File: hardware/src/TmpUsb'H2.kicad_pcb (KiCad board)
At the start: 2 copper layers, 26.5 x 17 mm, 20 parts, among them J1 215307, J2 292133-3, U1 PIC18F26J50

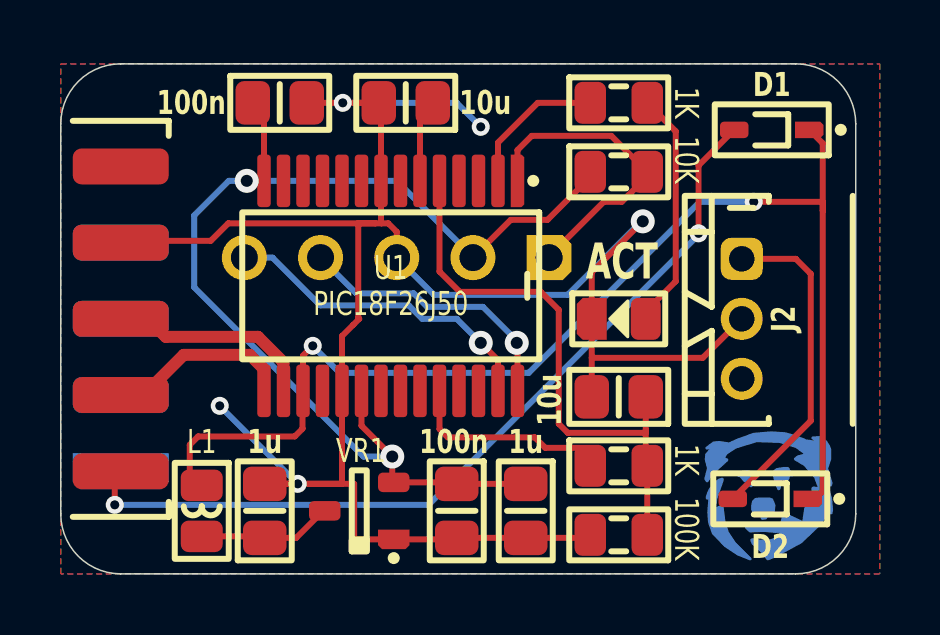
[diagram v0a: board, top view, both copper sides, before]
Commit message: Renamed V+ nets
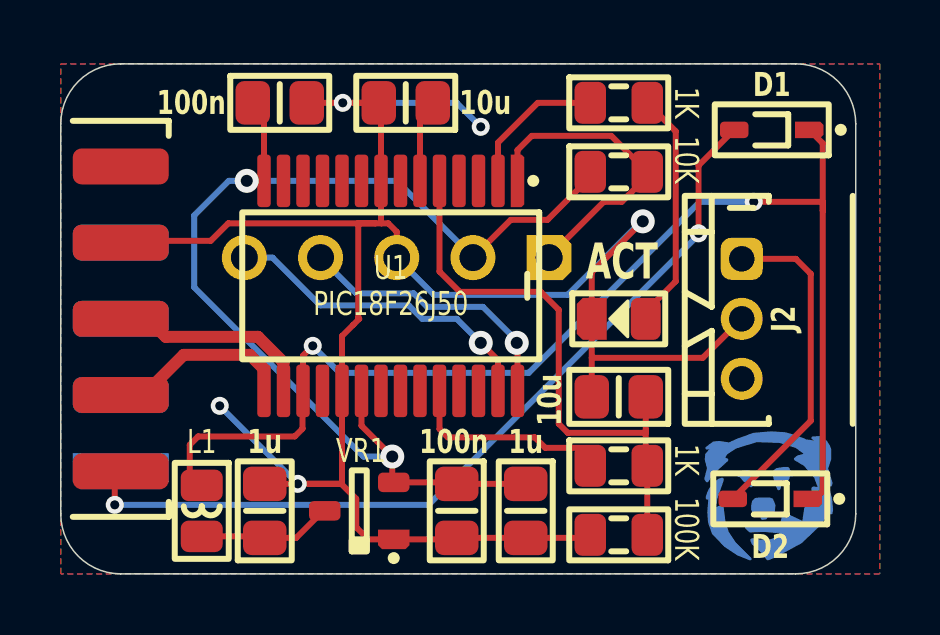
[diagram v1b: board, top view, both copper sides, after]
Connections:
- net +3.3V renamed 3V3
- net +5V renamed 5V
- net VCAP renamed 3V3_VCAP
- net VCC renamed 5V_IN
- net Vstby renamed 5V_STBY
- net Vusb renamed 5V_USB
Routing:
- net GND: track 74.4 -> 71.3 mm

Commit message: Swapping diodes around
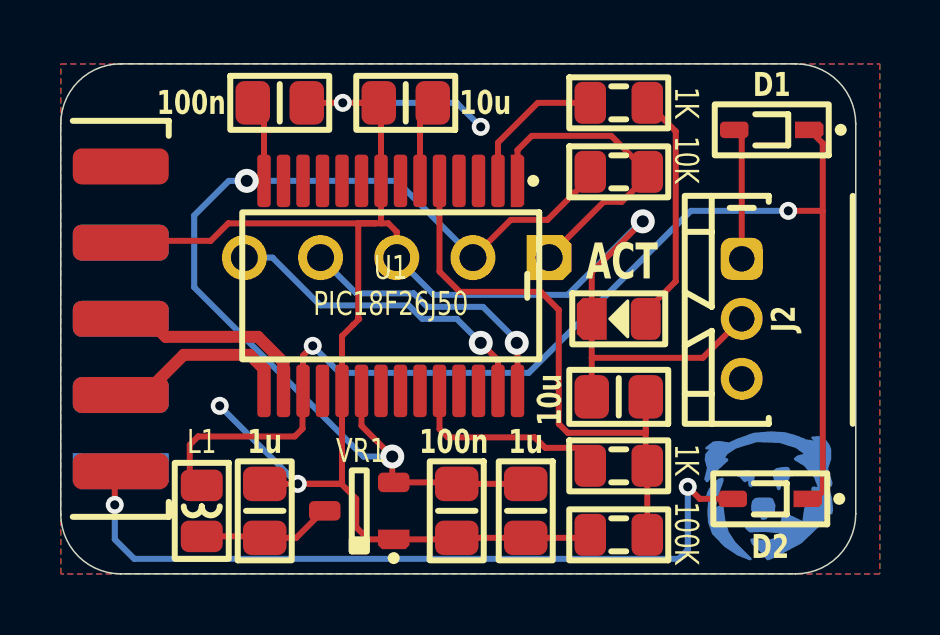
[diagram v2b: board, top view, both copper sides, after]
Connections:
- D1 pad 2: 5V_USB -> 5V_STBY
- D2 pad 2: 5V_STBY -> 5V_USB
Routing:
- net 5V_STBY: track 11.1 -> 4.40 mm
- net 5V_USB: track 28.3 -> 25.5 mm
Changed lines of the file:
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@@
 		)
 		(property "Value" "100K"
-			(at -2.25 0.2 -90)
+			(at -2.25 0.05 270)
 			(unlocked yes)
 			(layer "F.SilkS")
@@
 			(layers "F.Cu" "F.Paste" "F.Mask")
 			(roundrect_rratio 0.25)
-			(net 11 "5V_USB")
+			(net 15 "5V_STBY")
 			(thermal_bridge_angle 45)
 		)
@@
 			(layers "F.Cu" "F.Paste" "F.Mask")
 			(roundrect_rratio 0.25)
-			(net 15 "5V_STBY")
+			(net 11 "5V_USB")
 			(thermal_bridge_angle 45)
 		)
@@
 	)
 	(gr_text "TmpUsb'H2 BXXXX"
-		(at 28.2 30.7 0)
+		(at 26.2 23.9 0)
 		(layer "B.SilkS")
 		(effects
@@
 	)
 	(segment
-		(start 36.260361 18.389639)
-		(end 36.260361 20.65)
+		(start 36.3 29.5)
+		(end 35.9 29.1)
 		(width 0.2)
 		(layer "F.Cu")
@@
 	)
 	(segment
-		(start 37.45 17.2)
-		(end 36.260361 18.389639)
+		(start 37.4 29.5)
+		(end 36.3 29.5)
 		(width 0.2)
 		(layer "F.Cu")
@@
 	)
 	(via
-		(at 36.260361 20.65)
+		(at 35.9 29.1)
 		(size 0.6)
 		(drill 0.3)
@@
 	)
 	(segment
-		(start 36.260361 20.7003)
-		(end 36.260361 20.65)
+		(start 35.6 31.5)
+		(end 35.9 31.2)
+		(width 0.2)
+		(layer "B.Cu")
+		(net 11)
+	)
+	(segment
+		(start 35.9 31.2)
+		(end 35.9 29.1)
 		(width 0.2)
 		(layer "B.Cu")
@@
 	(segment
 		(start 16.8 29.7)
-		(end 27.260661 29.7)
+		(end 16.8 30.85)
 		(width 0.2)
 		(layer "B.Cu")
@@
 	)
 	(segment
-		(start 27.260661 29.7)
-		(end 36.260361 20.7003)
+		(start 17.45 31.5)
+		(end 35.6 31.5)
+		(width 0.2)
+		(layer "B.Cu")
+		(net 11)
+	)
+	(segment
+		(start 16.8 30.85)
+		(end 17.45 31.5)
 		(width 0.2)
 		(layer "B.Cu")
@@
 	)
 	(segment
-		(start 37.7 21.5)
-		(end 39.5 21.5)
-		(width 0.2)
-		(layer "F.Cu")
-		(net 15)
-	)
-	(segment
-		(start 39.5 21.5)
-		(end 40 22)
+		(start 37.7 17.45)
+		(end 37.45 17.2)
 		(width 0.2)
 		(layer "F.Cu")
@@
 	)
 	(segment
-		(start 40 22)
-		(end 40 26.9)
-		(width 0.2)
-		(layer "F.Cu")
-		(net 15)
-	)
-	(segment
-		(start 40 26.9)
-		(end 37.4 29.5)
+		(start 37.7 21.5)
+		(end 37.7 17.45)
 		(width 0.2)
 		(layer "F.Cu")
@@
 	)
 	(segment
-		(start 40.4 19.6)
-		(end 38.1 19.6)
+		(start 40.4 19.9)
+		(end 39.250008 19.9)
 		(width 0.2)
 		(layer "F.Cu")
@@
 	)
 	(segment
-		(start 40.4 19.9)
-		(end 40.4 19.6)
+		(start 39.250008 19.9)
+		(end 39.25 19.899992)
 		(width 0.2)
 		(layer "F.Cu")
@@
 	)
 	(via
-		(at 38.1 19.6)
+		(at 39.25 19.899992)
 		(size 0.6)
 		(drill 0.3)
@@
 	)
 	(segment
-		(start 36.3 19.6)
-		(end 38.1 19.6)
+		(start 24.3 25.3)
+		(end 30.6 25.3)
 		(width 0.2)
 		(layer "B.Cu")
@@
 	)
 	(segment
-		(start 24.3 25.3)
-		(end 30.6 25.3)
+		(start 30.6 25.3)
+		(end 36.000008 19.899992)
 		(width 0.2)
 		(layer "B.Cu")
@@
 	)
 	(segment
-		(start 30.6 25.3)
-		(end 36.3 19.6)
+		(start 36.000008 19.899992)
+		(end 39.25 19.899992)
 		(width 0.2)
 		(layer "B.Cu")

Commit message: Adjusted silkscreen
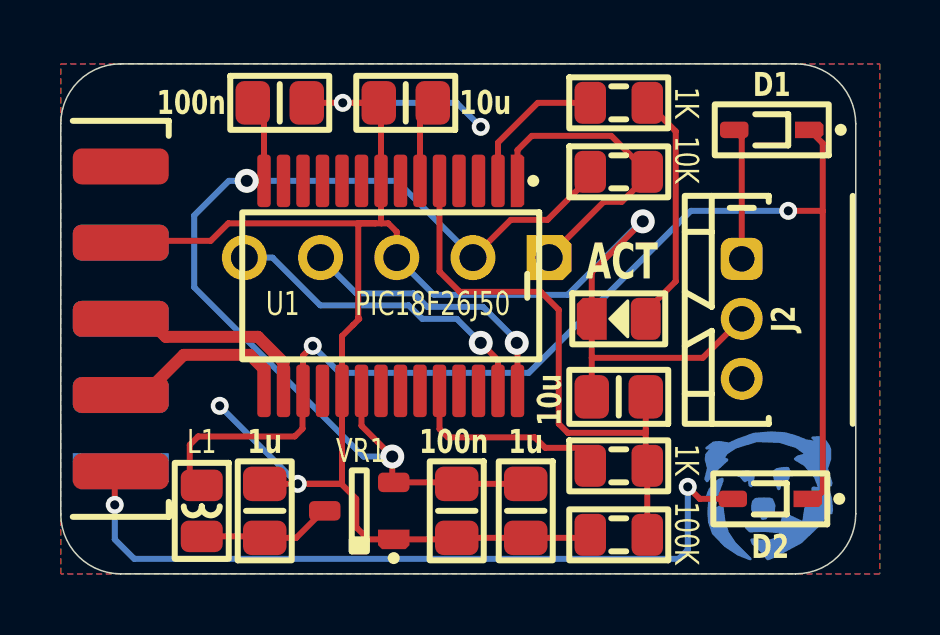
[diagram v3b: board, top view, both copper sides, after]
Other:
- board text added: "5V"
- board text added: "GND"
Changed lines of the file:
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@@
 		)
 		(property "Value" "100K"
-			(at -2.25 0.05 270)
+			(at -2.25 0.05 -90)
 			(unlocked yes)
 			(layer "F.SilkS")
@@
 				(font
 					(size 1.27 1.27)
+					(thickness 0.15)
 				)
 			)
@@
 				(font
 					(size 1.27 1.27)
+					(thickness 0.15)
 				)
 			)
@@
 				(font
 					(size 1.27 1.27)
+					(thickness 0.15)
 				)
 			)
@@
 				(font
 					(size 1.27 1.27)
+					(thickness 0.15)
 				)
 			)
@@
 				(font
 					(size 1.27 1.27)
+					(thickness 0.15)
 				)
 			)
@@
 				(font
 					(size 1.27 1.27)
+					(thickness 0.15)
 				)
 			)
@@
 				(font
 					(size 1.27 1.27)
+					(thickness 0.15)
 				)
 			)
@@
 				(font
 					(size 1.27 1.27)
+					(thickness 0.15)
 				)
 			)
@@
 				(font
 					(size 1.27 1.27)
+					(thickness 0.15)
 				)
 			)
@@
 				(font
 					(size 1.27 1.27)
+					(thickness 0.15)
 				)
 			)
@@
 				(font
 					(size 1.27 1.27)
+					(thickness 0.15)
 				)
 			)
@@
 				(font
 					(size 1.27 1.27)
+					(thickness 0.15)
 				)
 			)
@@
 				(font
 					(size 1.27 1.27)
+					(thickness 0.15)
 				)
 			)
@@
 				(font
 					(size 1.27 1.27)
+					(thickness 0.15)
 				)
 			)
@@
 				(font
 					(size 1.27 1.27)
+					(thickness 0.15)
 				)
 			)
@@
 				(font
 					(size 1.27 1.27)
+					(thickness 0.15)
 				)
 			)
@@
 				(font
 					(size 1.27 1.27)
+					(thickness 0.15)
 				)
 			)
@@
 				(font
 					(size 1.27 1.27)
+					(thickness 0.15)
 				)
 			)
@@
 				(font
 					(size 1.27 1.27)
+					(thickness 0.15)
 				)
 			)
@@
 				(font
 					(size 1.27 1.27)
+					(thickness 0.15)
 				)
 			)
@@
 				(font
 					(size 1.27 1.27)
+					(thickness 0.15)
 				)
 			)
@@
 				(font
 					(size 1.27 1.27)
+					(thickness 0.15)
 				)
 			)
@@
 				(font
 					(size 1.27 1.27)
+					(thickness 0.15)
 				)
 			)
@@
 				(font
 					(size 1.27 1.27)
+					(thickness 0.15)
 				)
 			)
@@
 				(font
 					(size 1.27 1.27)
+					(thickness 0.15)
 				)
 			)
@@
 				(font
 					(size 1.27 1.27)
+					(thickness 0.15)
 				)
 			)
@@
 				(font
 					(size 1.27 1.27)
+					(thickness 0.15)
 				)
 			)
@@
 				(font
 					(size 1.27 1.27)
+					(thickness 0.15)
 				)
 			)
@@
 				(font
 					(size 1.27 1.27)
+					(thickness 0.15)
 				)
 			)
@@
 				(font
 					(size 1.27 1.27)
+					(thickness 0.15)
 				)
 			)
@@
 				(font
 					(size 1.27 1.27)
+					(thickness 0.15)
 				)
 			)
@@
 				(font
 					(size 1.27 1.27)
+					(thickness 0.15)
 				)
 			)
@@
 				(font
 					(size 1.27 1.27)
+					(thickness 0.15)
 				)
 			)
@@
 				(font
 					(size 1.27 1.27)
+					(thickness 0.15)
 				)
 			)
@@
 				(font
 					(size 1.27 1.27)
+					(thickness 0.15)
 				)
 			)
@@
 				(font
 					(size 1.27 1.27)
+					(thickness 0.15)
 				)
 			)
@@
 				(font
 					(size 1.27 1.27)
+					(thickness 0.15)
 				)
 			)
@@
 				(font
 					(size 1.27 1.27)
+					(thickness 0.15)
 				)
 			)
@@
 				(font
 					(size 1.27 1.27)
+					(thickness 0.15)
 				)
 			)
@@
 				(font
 					(size 1.27 1.27)
+					(thickness 0.15)
 				)
 			)
@@
 				(font
 					(size 1.27 1.27)
+					(thickness 0.15)
 				)
 			)
@@
 				(font
 					(size 1.27 1.27)
+					(thickness 0.15)
 				)
 			)
@@
 		(tags "SOP65P775X200-28N")
 		(property "Reference" "U1"
-			(at -0.6 0 0)
+			(at 0.6 3.6 0)
 			(layer "F.SilkS")
 			(effects
@@
 		)
 		(property "Value" "PIC18F26J50"
-			(at 0.6 0 0)
+			(at 0.6 -1.4 0)
 			(layer "F.SilkS")
 			(effects
@@
 				(font
 					(size 1.27 1.27)
+					(thickness 0.15)
 				)
 			)
@@
 				(font
 					(size 1.27 1.27)
+					(thickness 0.15)
 				)
 			)
@@
 				(font
 					(size 1.27 1.27)
+					(thickness 0.15)
 				)
 			)
@@
 				(font
 					(size 1.27 1.27)
+					(thickness 0.15)
 				)
 			)
@@
 				(font
 					(size 1.27 1.27)
+					(thickness 0.15)
 				)
 			)
@@
 				(font
 					(size 1.27 1.27)
+					(thickness 0.15)
 				)
 			)
@@
 				(font
 					(size 1.27 1.27)
+					(thickness 0.15)
 				)
 			)
@@
 				(font
 					(size 1.27 1.27)
+					(thickness 0.15)
 				)
 			)
@@
 				(font
 					(size 1.27 1.27)
+					(thickness 0.15)
 				)
 			)
@@
 				(font
 					(size 1.27 1.27)
+					(thickness 0.15)
 				)
 			)
@@
 				(font
 					(size 1.27 1.27)
+					(thickness 0.15)
 				)
 			)
@@
 				(font
 					(size 1.27 1.27)
+					(thickness 0.15)
 				)
 			)
@@
 				(font
 					(size 1.27 1.27)
+					(thickness 0.15)
 				)
 			)
@@
 				(font
 					(size 1.27 1.27)
+					(thickness 0.15)
 				)
 			)
@@
 				(font
 					(size 1.27 1.27)
+					(thickness 0.15)
 				)
 			)
@@
 				(font
 					(size 1.27 1.27)
+					(thickness 0.15)
 				)
 				(justify mirror)
@@
 				(font
 					(size 1.27 1.27)
+					(thickness 0.15)
 				)
 				(justify mirror)
@@
 				(font
 					(size 1.27 1.27)
+					(thickness 0.15)
 				)
 				(justify mirror)
@@
 			)
 			(justify mirror)
+		)
+	)
+	(gr_text "GND"
+		(at 39.5 23.5 90)
+		(layer "B.SilkS")
+		(effects
+			(font
+				(size 0.8 0.6)
+				(thickness 0.15)
+				(bold yes)
+			)
+			(justify mirror)
+		)
+	)
+	(gr_text "5V"
+		(at 39.5 21.5 90)
+		(layer "B.SilkS")
+		(effects
+			(font
+				(size 0.8 0.6)
+				(thickness 0.15)
+				(bold yes)
+			)
+			(justify mirror)
